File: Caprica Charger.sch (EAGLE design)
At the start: 60 parts, among them J1 POWER_JACKPTH, Q4 MOSFET, Q5 MOSFET

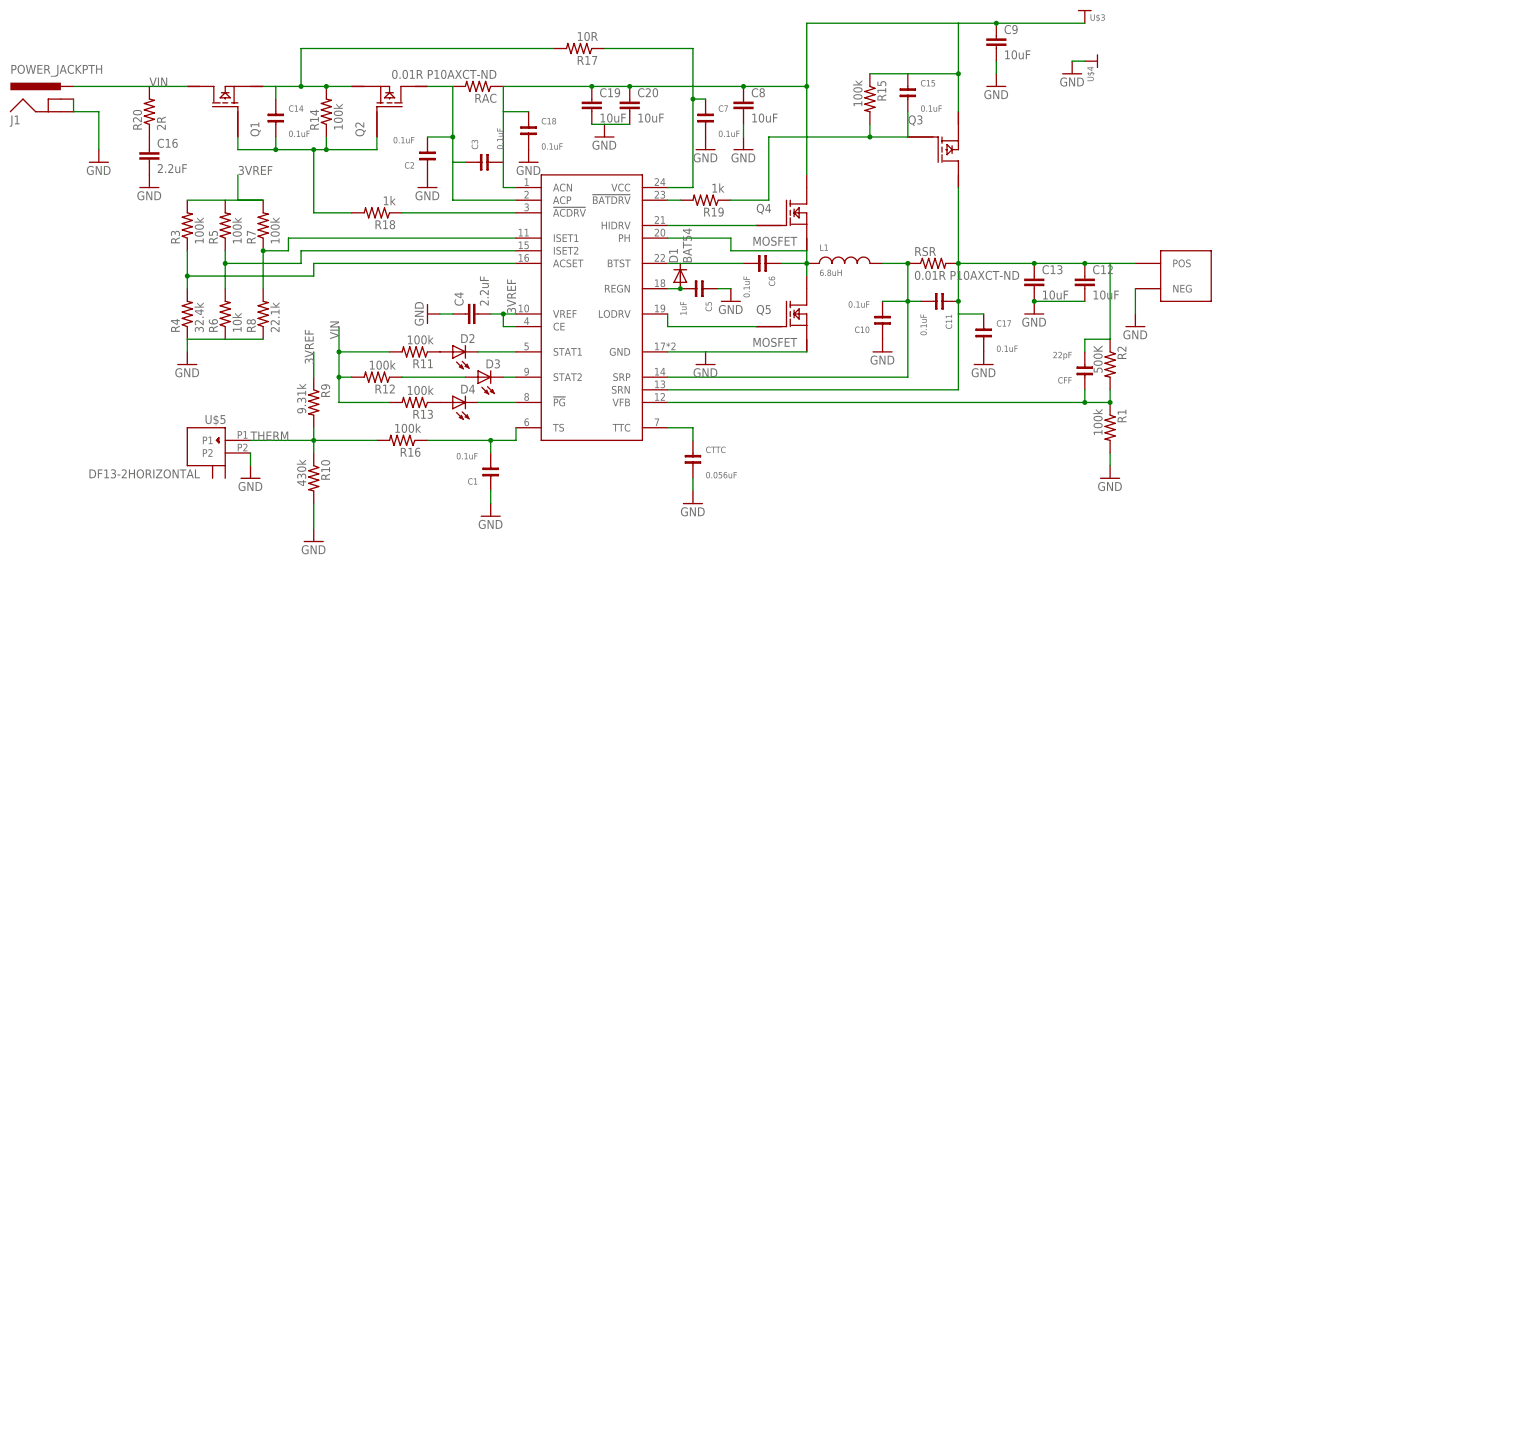
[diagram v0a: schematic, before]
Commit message: Balancing added and all laid out. Still may be all wrong.
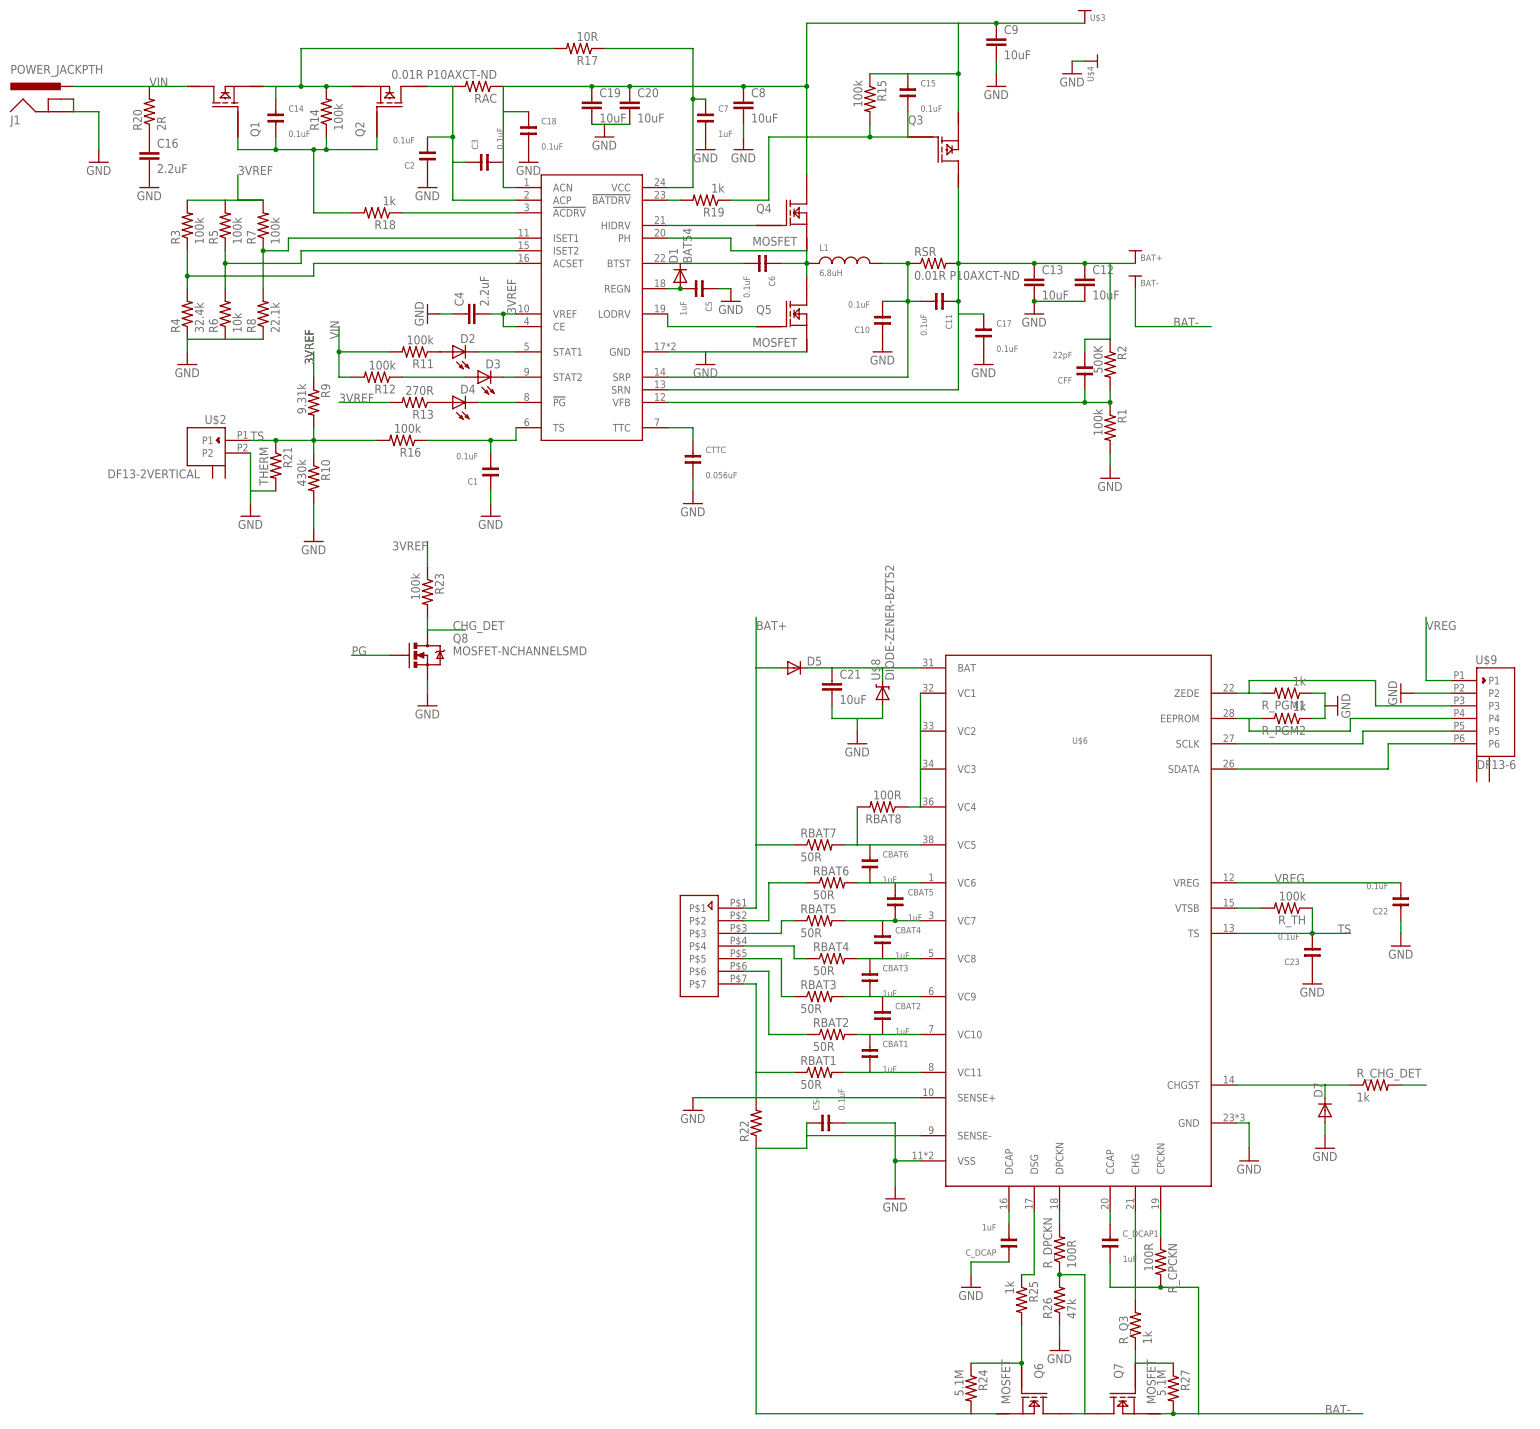
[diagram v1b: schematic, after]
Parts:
- removed U$5: DF13-2HORIZONTAL, Taylor:DF13-2HORIZONTAL
- added BAT+, BAT-: HIGHCURRENTPAD2, Taylor:HIGHCURRENTPAD2
- added C21: 10uF, SparkFun:CAP1206
- added C22, C23, CS-: 0.1uF, Taylor:CAPACITOR0603-CAP
- added CBAT1, CBAT2, CBAT3, CBAT4, CBAT5, CBAT6, C_DCAP, C_DCAP1: 1uF, Taylor:CAPACITOR0603-CAP
- added D5: (no value), SparkFun:DIODESMA
- added D7: (no value), SparkFun:DIODESOD
- added Q6, Q7: MOSFET, Taylor:MOSFET
- added Q8: MOSFET-NCHANNELSMD, SparkFun:MOSFET-NCHANNELSMD
- added R21: THERM, Taylor:RESISTOR
- added R22: (no value), Taylor:RESISTOROHMITE
- added R23, R_TH: 100k, Taylor:RESISTOR
- added R24, R27: 5.1M, Taylor:RESISTOR
- added R25, R_CHG_DET, R_PGM1, R_PGM2, R_Q3: 1k, Taylor:RESISTOR
- added R26: 47k, Taylor:RESISTOR
- added RBAT1, RBAT2, RBAT3, RBAT4, RBAT5, RBAT6, RBAT7: 50R, Taylor:RESISTOR
- added RBAT8, R_CPCKN, R_DPCKN: 100R, Taylor:RESISTOR
- added U$6: BQ77910A_BATTERY_PROTECTOR, Taylor:BQ77910A_BATTERY_PROTECTOR
- added U$7: JST_XH_7, Taylor:JST_XH_7
- added U$8: DIODE-ZENER-BZT52, SparkFun:DIODE-ZENER-BZT52
- added U$9: DF13-6, Taylor:DF13-6
- C7: value 0.1uF -> 1uF
- R13: value 100k -> 270R
- U$2: value XT60 -> DF13-2VERTICAL; device Taylor:XT60 -> Taylor:DF13-2VERTICAL
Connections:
- net N$22 renamed HIDRV
- net SYS renamed SYS+
- removed net BAT: C11.1, C12.1, C13.1, C17.1, CFF.2, Q3.DRAIN, R2.1, RSR.2, U$1.SRN, U$2.POS
- removed net THERM: R10.1, R16.2, R9.2, U$5.P1
- new net BAT+: BAT+.P$1, C11.1, C12.1, C13.1, C17.1, CFF.2, D5.A, Q3.DRAIN, R2.1, RBAT7.1, RSR.2, U$1.SRN, U$7.P$1
- new net BAT-: BAT-.P$1, C_DCAP1.2, Q7.S@1, R27.2, R_CPCKN.2
- new net CHG_DET: Q8.D, R23.2, R_CHG_DET.2
- new net N$17: CBAT2.1, CBAT3.2, RBAT3.2, U$6.VC9
- new net N$22: CBAT3.1, CBAT4.2, RBAT4.2, U$6.VC8
- new net N$23: CBAT1.2, RBAT1.2, U$6.VC11
- new net N$29: CBAT5.1, CBAT6.2, RBAT6.2, U$6.VC6
- new net N$31: CBAT4.1, CBAT5.2, RBAT5.2, U$6.VC7
- new net N$32: C_DCAP.2, U$6.DCAP
- new net N$33: CBAT6.1, RBAT7.2, RBAT8.2, U$6.VC5
- new net N$34: RBAT8.1, U$6.VC1, U$6.VC2, U$6.VC3, U$6.VC4
- new net N$35: C21.1, D5.C, U$6.BAT, U$8.C
- new net N$37: D7.C, R_CHG_DET.1, U$6.CHGST
- new net N$38: RBAT2.1, U$7.P$6
- new net N$39: RBAT3.1, U$7.P$5
- new net N$40: RBAT4.1, U$7.P$4
- new net N$41: Q6.G@1, R24.1, R25.2
- new net N$42: RBAT6.1, U$7.P$2
- new net N$43: RBAT5.1, U$7.P$3
- new net N$44: R_DPCKN.2, U$6.DPCKN
- new net N$46: Q6.D@25, Q7.D@25, R26.2, R_DPCKN.1
- new net N$47: U$6.SCLK, U$9.P5
- new net N$48: CS-.1, Q6.S@1, R22.1, R24.2, U$6.SENSE-
- new net N$49: C_DCAP1.1, U$6.CCAP
- new net N$5: CBAT1.1, CBAT2.2, RBAT2.2, U$6.VC10
- new net N$50: R_Q3.2, U$6.CHG
- new net N$51: Q7.G@1, R27.1, R_Q3.1
- new net N$52: U$6.SDATA, U$9.P6
- new net N$53: R_CPCKN.1, U$6.CPCKN
- new net N$54: R_PGM2.2, U$6.EEPROM, U$9.P4
- new net N$55: R_TH.2, U$6.VTSB
- new net N$57: R_PGM1.2, U$6.ZEDE, U$9.P3
- new net PG: D4.C, Q8.G, U$1.!PG!
- new net TS: C23.2, R10.1, R16.2, R21.1, R9.2, R_TH.1, U$2.P1, U$6.TS
- new net VREG: C22.2, U$6.VREG, U$9.P1
- net 3VREF: now also R13.2, R23.1
- net GND: now also C21.2, C22.1, C23.1, CS-.2, C_DCAP.1, D7.A, Q8.S, R21.2, R22.2, R26.1, RBAT1.1, R_PGM1.1, R_PGM2.1, U$2.P2, U$6.GND, U$6.SENSE+, U$6.VSS, U$7.P$7, U$8.A, U$9.P2; no longer U$2.NEG, U$5.P2
- net N$12: now also R25.1, U$6.DSG; no longer D4.C, U$1.!PG!
- net VIN: no longer R13.2
